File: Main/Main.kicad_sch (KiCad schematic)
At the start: 76 parts, among them J1 USB_B_Micro, J2 Micro_SD_Card, J3 Conn_01x03, J4 Conn_01x03, J5 Conn_01x03, J6 Conn_01x03, SW1 SW_Push, SW2 SW_Push, U1 RP2350A-QFN60, U10 LM75B, U11 MCS1802GS-50-Z, U12 MCS1802GS-50-Z, U13 MCS1802GS-50-Z, U2 W25Q128JVS, U3 AMS1117-3.3, U4 MMC5983MA, U5 ICM-42688-P, U6 INA226, U7 KX134-1211, U8 MS5611-01BA, U9 MCS1802GS-50-Z, Y1 ABM8-272-T3

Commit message: Layout/Footprint Updates
updated footprint of inductor for R-Pi, started planning layout for R-PI components in middle of board, added two options for board size
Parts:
- C10, C11, C12, C13, C14, C15, C16, C17, C18, C19, C20, C21, C22, C23, C24, C25, C26, C27, C28, C29, C30, C31, C32, C33, C34, C5, C6, C7, C8, C9: footprint Capacitor_SMD:C_0805_2012Metric -> Capacitor_SMD:C_0603_1608Metric
- L1: footprint Inductor_SMD:L_0805_2012Metric -> otherComponents:AOTA-B201610S3R3-101-T(L_0806_2016metric)
- R10, R11, R12, R2, R3, R4, R5, R6, R7, R8: footprint Resistor_SMD:R_0805_2012Metric -> Resistor_SMD:R_0603_1608Metric
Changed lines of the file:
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@@
 			)
 		)
-		(property "Footprint" "Capacitor_SMD:C_0805_2012Metric"
+		(property "Footprint" "Capacitor_SMD:C_0603_1608Metric"
 			(at 262.5852 38.1 0)
 			(effects
@@
 			)
 		)
-		(property "Footprint" "Resistor_SMD:R_0805_2012Metric"
+		(property "Footprint" "Resistor_SMD:R_0603_1608Metric"
 			(at 133.35 117.348 90)
 			(effects
@@
 			)
 		)
-		(property "Footprint" "Capacitor_SMD:C_0805_2012Metric"
+		(property "Footprint" "Capacitor_SMD:C_0603_1608Metric"
 			(at 126.6952 38.1 0)
 			(effects
@@
 			)
 		)
-		(property "Footprint" "Capacitor_SMD:C_0805_2012Metric"
+		(property "Footprint" "Capacitor_SMD:C_0603_1608Metric"
 			(at 205.4352 38.1 0)
 			(effects
@@
 			)
 		)
-		(property "Footprint" "Capacitor_SMD:C_0805_2012Metric"
+		(property "Footprint" "Capacitor_SMD:C_0603_1608Metric"
 			(at 352.7552 46.99 0)
 			(effects
@@
 			)
 		)
-		(property "Footprint" "Capacitor_SMD:C_0805_2012Metric"
+		(property "Footprint" "Capacitor_SMD:C_0603_1608Metric"
 			(at 293.0652 38.1 0)
 			(effects
@@
 			)
 		)
-		(property "Footprint" "Capacitor_SMD:C_0805_2012Metric"
+		(property "Footprint" "Capacitor_SMD:C_0603_1608Metric"
 			(at 21.8948 203.2 0)
 			(effects
@@
 			)
 		)
-		(property "Footprint" "Capacitor_SMD:C_0805_2012Metric"
+		(property "Footprint" "Capacitor_SMD:C_0603_1608Metric"
 			(at 378.1552 111.76 0)
 			(effects
@@
 			)
 		)
-		(property "Footprint" "Resistor_SMD:R_0805_2012Metric"
+		(property "Footprint" "Resistor_SMD:R_0603_1608Metric"
 			(at 435.61 84.328 90)
 			(effects
@@
 			)
 		)
-		(property "Footprint" "Capacitor_SMD:C_0805_2012Metric"
+		(property "Footprint" "Capacitor_SMD:C_0603_1608Metric"
 			(at 119.0752 335.28 0)
 			(effects
@@
 			)
 		)
-		(property "Footprint" "Capacitor_SMD:C_0805_2012Metric"
+		(property "Footprint" "Capacitor_SMD:C_0603_1608Metric"
 			(at 115.57 204.7748 0)
 			(effects
@@
 			)
 		)
-		(property "Footprint" "Resistor_SMD:R_0805_2012Metric"
+		(property "Footprint" "Resistor_SMD:R_0603_1608Metric"
 			(at 53.34 112.268 90)
 			(effects
@@
 			)
 		)
-		(property "Footprint" "Capacitor_SMD:C_0805_2012Metric"
+		(property "Footprint" "Capacitor_SMD:C_0603_1608Metric"
 			(at 239.7252 38.1 0)
 			(effects
@@
 			)
 		)
-		(property "Footprint" "Capacitor_SMD:C_0805_2012Metric"
+		(property "Footprint" "Capacitor_SMD:C_0603_1608Metric"
 			(at 352.7552 201.93 0)
 			(effects
@@
 			)
 		)
-		(property "Footprint" "Capacitor_SMD:C_0805_2012Metric"
+		(property "Footprint" "Capacitor_SMD:C_0603_1608Metric"
 			(at 119.0752 276.86 0)
 			(effects
@@
 			)
 		)
-		(property "Footprint" "Inductor_SMD:L_0805_2012Metric"
+		(property "Footprint" "otherComponents:AOTA-B201610S3R3-101-T(L_0806_2016metric)"
 			(at 125.73 71.12 0)
 			(effects
@@
 			)
 		)
-		(property "Footprint" "Capacitor_SMD:C_0805_2012Metric"
+		(property "Footprint" "Capacitor_SMD:C_0603_1608Metric"
 			(at 113.03 114.6048 0)
 			(effects
@@
 			)
 		)
-		(property "Footprint" "Resistor_SMD:R_0805_2012Metric"
+		(property "Footprint" "Resistor_SMD:R_0603_1608Metric"
 			(at 129.54 122.428 90)
 			(effects
@@
 			)
 		)
-		(property "Footprint" "Capacitor_SMD:C_0805_2012Metric"
+		(property "Footprint" "Capacitor_SMD:C_0603_1608Metric"
 			(at 194.0052 38.1 0)
 			(effects
@@
 			)
 		)
-		(property "Footprint" "Resistor_SMD:R_0805_2012Metric"
+		(property "Footprint" "Resistor_SMD:R_0603_1608Metric"
 			(at 229.87 66.548 90)
 			(effects
@@
 			)
 		)
-		(property "Footprint" "Capacitor_SMD:C_0805_2012Metric"
+		(property "Footprint" "Capacitor_SMD:C_0603_1608Metric"
 			(at 234.6452 335.28 0)
 			(effects
@@
 			)
 		)
-		(property "Footprint" "Capacitor_SMD:C_0805_2012Metric"
+		(property "Footprint" "Capacitor_SMD:C_0603_1608Metric"
 			(at 289.2552 208.28 0)
 			(effects
@@
 			)
 		)
-		(property "Footprint" "Capacitor_SMD:C_0805_2012Metric"
+		(property "Footprint" "Capacitor_SMD:C_0603_1608Metric"
 			(at 248.6152 195.58 0)
 			(effects
@@
 			)
 		)
-		(property "Footprint" "Capacitor_SMD:C_0805_2012Metric"
+		(property "Footprint" "Capacitor_SMD:C_0603_1608Metric"
 			(at 182.5752 38.1 0)
 			(effects
@@
 			)
 		)
-		(property "Footprint" "Capacitor_SMD:C_0805_2012Metric"
+		(property "Footprint" "Capacitor_SMD:C_0603_1608Metric"
 			(at 404.8252 194.31 0)
 			(effects
@@
 			)
 		)
-		(property "Footprint" "Resistor_SMD:R_0805_2012Metric"
+		(property "Footprint" "Resistor_SMD:R_0603_1608Metric"
 			(at 435.61 95.758 90)
 			(effects
@@
 			)
 		)
-		(property "Footprint" "Capacitor_SMD:C_0805_2012Metric"
+		(property "Footprint" "Capacitor_SMD:C_0603_1608Metric"
 			(at 232.1052 276.86 0)
 			(effects
@@
 			)
 		)
-		(property "Footprint" "Capacitor_SMD:C_0805_2012Metric"
+		(property "Footprint" "Capacitor_SMD:C_0603_1608Metric"
 			(at 216.8652 38.1 0)
 			(effects
@@
 			)
 		)
-		(property "Footprint" "Capacitor_SMD:C_0805_2012Metric"
+		(property "Footprint" "Capacitor_SMD:C_0603_1608Metric"
 			(at 36.5252 72.39 0)
 			(effects
@@
 			)
 		)
-		(property "Footprint" "Capacitor_SMD:C_0805_2012Metric"
+		(property "Footprint" "Capacitor_SMD:C_0603_1608Metric"
 			(at 51.7652 36.83 0)
 			(effects
@@
 			)
 		)
-		(property "Footprint" "Resistor_SMD:R_0805_2012Metric"
+		(property "Footprint" "Resistor_SMD:R_0603_1608Metric"
 			(at 432.562 44.45 90)
 			(effects
@@
 			)
 		)
-		(property "Footprint" "Resistor_SMD:R_0805_2012Metric"
+		(property "Footprint" "Resistor_SMD:R_0603_1608Metric"
 			(at 435.61 72.898 90)
 			(effects
@@
 			)
 		)
-		(property "Footprint" "Capacitor_SMD:C_0805_2012Metric"
+		(property "Footprint" "Capacitor_SMD:C_0603_1608Metric"
 			(at 275.2852 38.1 0)
 			(effects
@@
 			)
 		)
-		(property "Footprint" "Capacitor_SMD:C_0805_2012Metric"
+		(property "Footprint" "Capacitor_SMD:C_0603_1608Metric"
 			(at 80.9752 36.83 0)
 			(effects
@@
 			)
 		)
-		(property "Footprint" "Capacitor_SMD:C_0805_2012Metric"
+		(property "Footprint" "Capacitor_SMD:C_0603_1608Metric"
 			(at 235.9152 195.58 0)
 			(effects
@@
 			)
 		)
-		(property "Footprint" "Resistor_SMD:R_0805_2012Metric"
+		(property "Footprint" "Resistor_SMD:R_0603_1608Metric"
 			(at 442.722 44.45 90)
 			(effects
@@
 			)
 		)
-		(property "Footprint" "Capacitor_SMD:C_0805_2012Metric"
+		(property "Footprint" "Capacitor_SMD:C_0603_1608Metric"
 			(at 228.2952 38.1 0)
 			(effects
@@
 			)
 		)
-		(property "Footprint" "Capacitor_SMD:C_0805_2012Metric"
+		(property "Footprint" "Capacitor_SMD:C_0603_1608Metric"
 			(at 138.1252 38.1 0)
 			(effects
@@
 			)
 		)
-		(property "Footprint" "Capacitor_SMD:C_0805_2012Metric"
+		(property "Footprint" "Capacitor_SMD:C_0603_1608Metric"
 			(at 251.1552 38.1 0)
 			(effects
@@
 			)
 		)
-		(property "Footprint" "Resistor_SMD:R_0805_2012Metric"
+		(property "Footprint" "Resistor_SMD:R_0603_1608Metric"
 			(at 229.87 55.118 90)
 			(effects
@@
 			)
 		)
-		(property "Footprint" "Capacitor_SMD:C_0805_2012Metric"
+		(property "Footprint" "Capacitor_SMD:C_0603_1608Metric"
 			(at 113.03 100.6348 0)
 			(effects

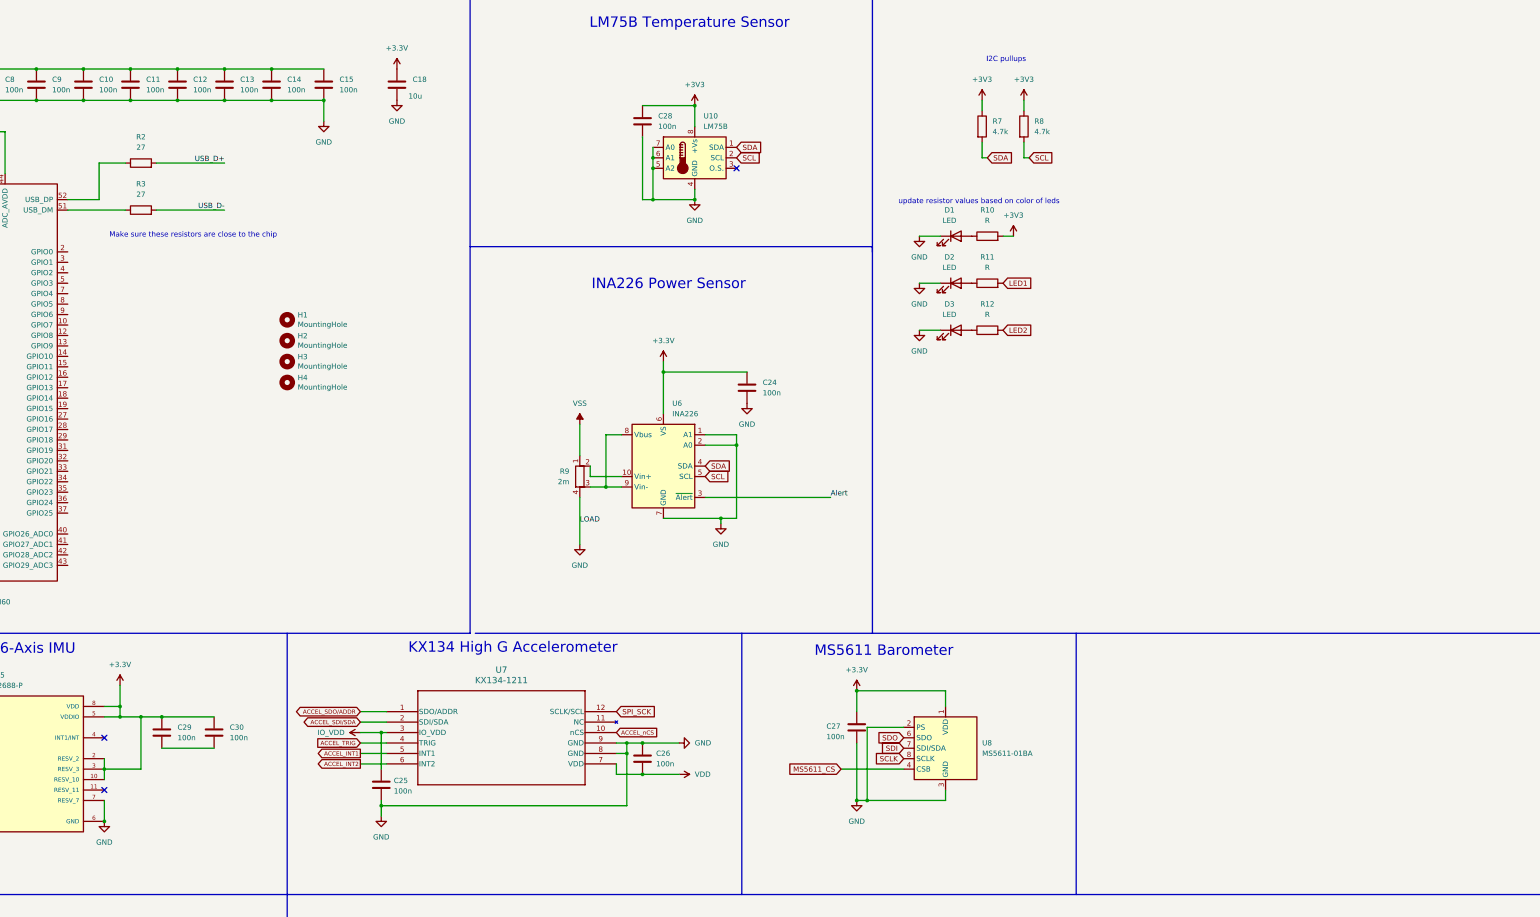
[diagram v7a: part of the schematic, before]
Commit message: More RP2350 Footprint
put more footprints in place(mostly power), updated things to 0402 where possible, and added switching regulator to schematic
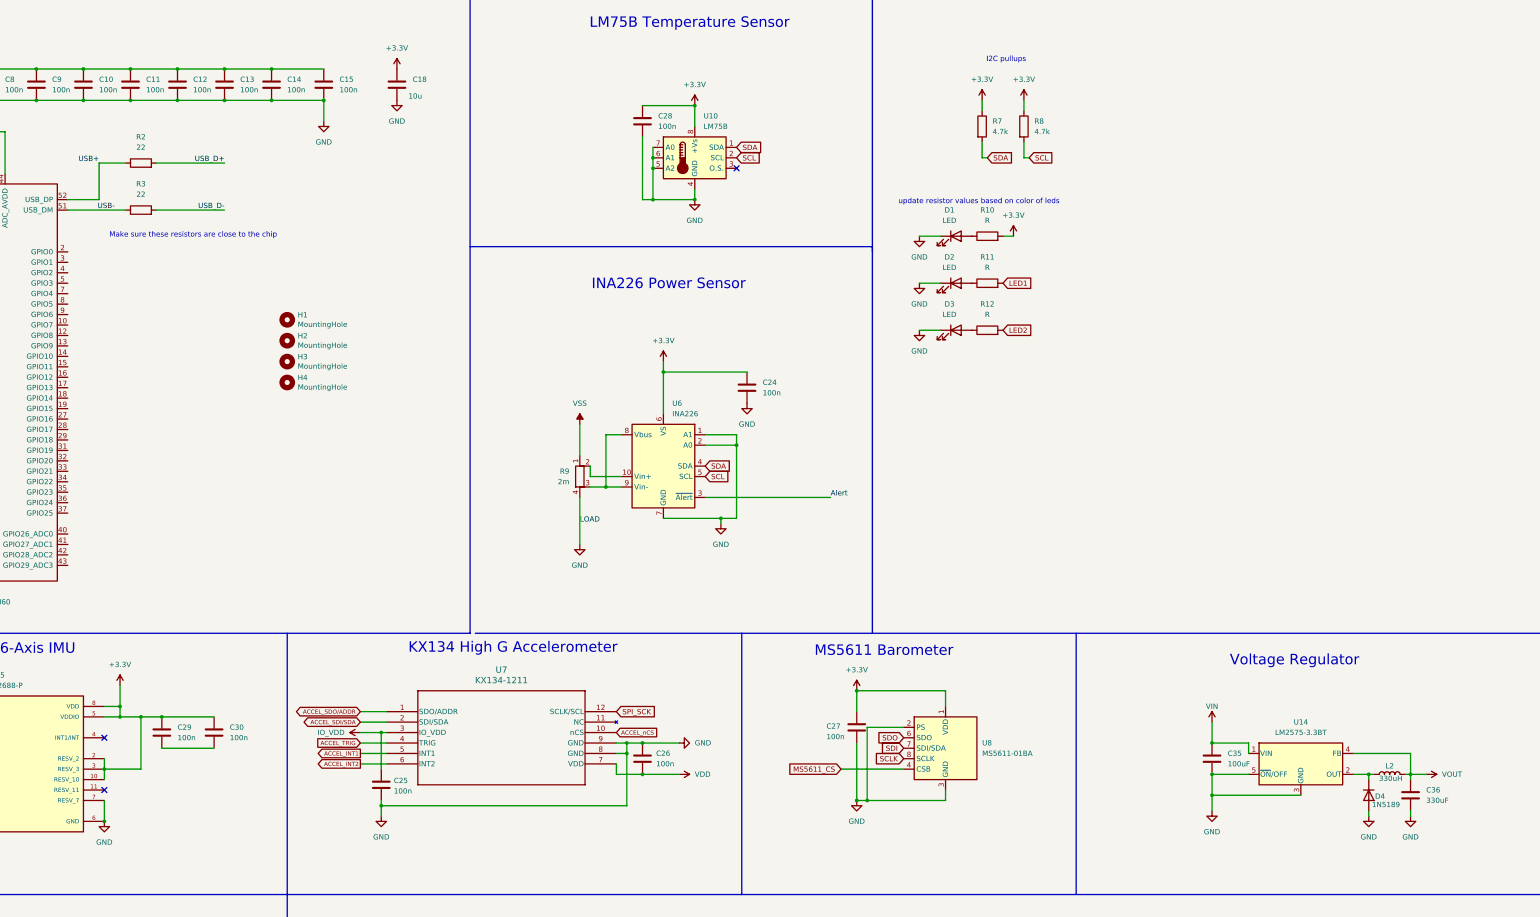
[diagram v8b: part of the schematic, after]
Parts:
- added C35: 100uF, Capacitor_SMD:C_0805_2012Metric, symbol Device:C
- added C36: 330uF, Capacitor_SMD:C_0805_2012Metric, symbol Device:C
- added D4: 1N5189, Diode_SMD:D_0805_2012Metric, symbol Device:D
- added L2: 330uH, Inductor_SMD:L_0805_2012Metric, symbol Device:L
- added U14: LM2575-3.3BT, Package_TO_SOT_SMD:TO-263-5_TabPin3, symbol Regulator_Switching:LM2575-3.3BT
- C10, C11, C12, C13, C14, C15, C16, C17, C19, C24, C25, C26, C27, C28, C29, C30, C31, C32, C33, C34, C5, C6, C7, C8, C9: footprint Capacitor_SMD:C_0603_1608Metric -> Capacitor_SMD:C_0402_1005Metric
- C18, C20, C21, C22, C23: footprint Capacitor_SMD:C_0603_1608Metric -> Capacitor_SMD:C_0805_2012Metric
- R10, R11, R12, R4, R5, R6, R7, R8: footprint Resistor_SMD:R_0603_1608Metric -> Resistor_SMD:R_0402_1005Metric
- R2, R3: value 27 -> 22; footprint Resistor_SMD:R_0603_1608Metric -> Resistor_SMD:R_0402_1005Metric
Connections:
- net +3V3 is gone; now on net +3.3V: C28.1, R10.2, R7.1, R8.1, U10.8 (+Vs)
- net GND: now also C35.2, C36.2, D4.2 (A), U14.3 (GND), U14.5 (~{ON}/OFF)
- net USB-: now reaches R3.1, U1.51 (USB_DM)
- net USB+: now reaches R2.1, U1.52 (USB_DP)
- new net: D4.1 (K), L2.1, U14.2 (OUT)
- new net VIN: C35.1, U14.1 (VIN)
- new net VOUT: C36.1, L2.2, U14.4 (FB)
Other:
- note added: "Voltage Regulator"
